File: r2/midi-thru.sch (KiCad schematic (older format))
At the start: 31 parts, among them J1 Barrel_Jack_Switch, J2 MIDI IN, J4 MIDI THRU3, J5 MIDI THRU1, J6 MIDI THRU2, J7 MIDI THRU3, U2 6N138, U3 74HC14

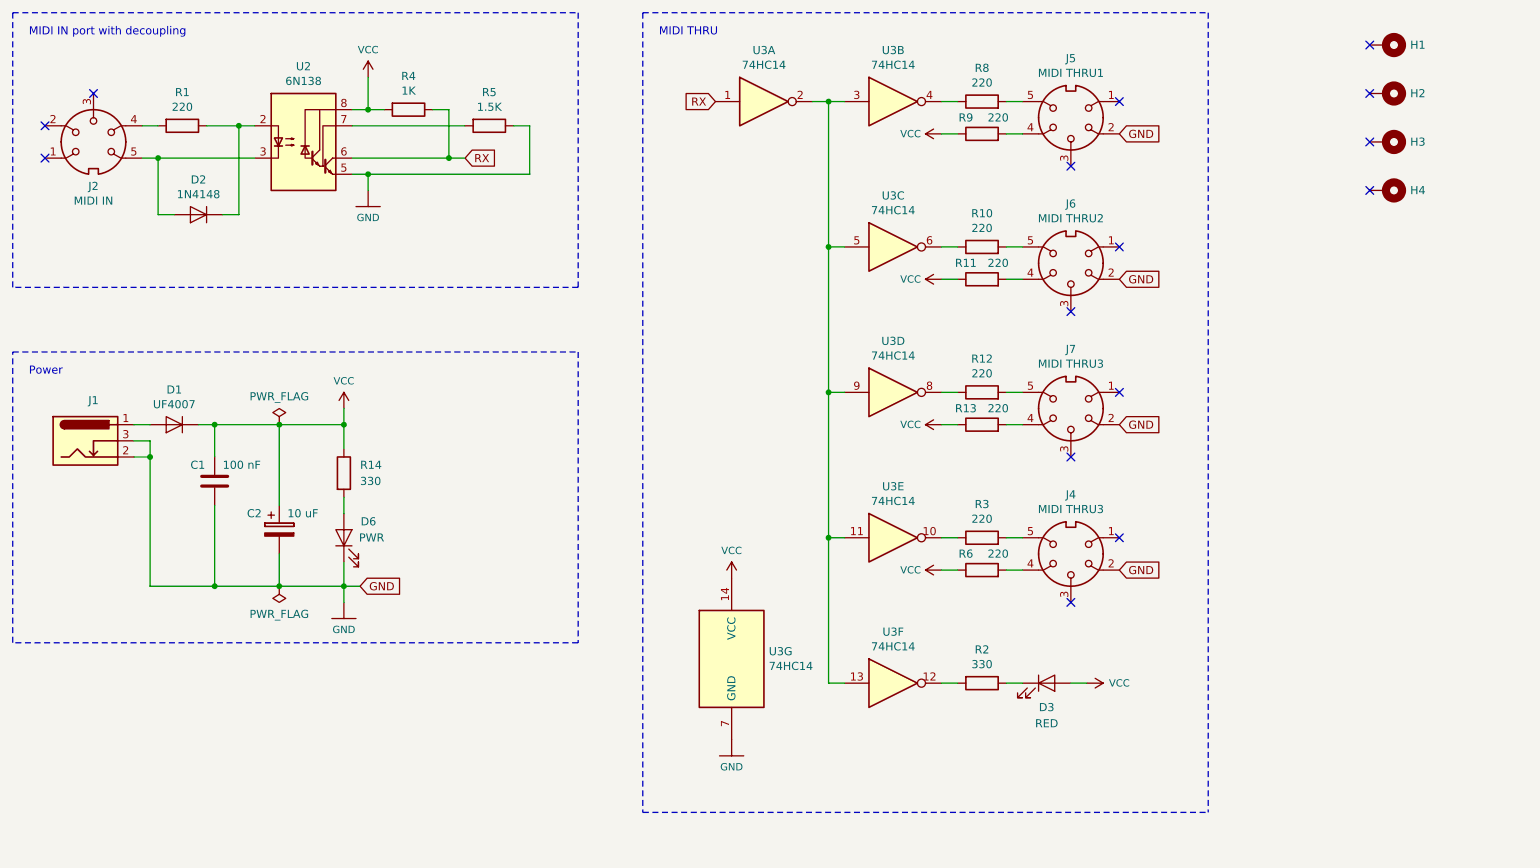
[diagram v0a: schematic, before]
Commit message: Add voltage regulator
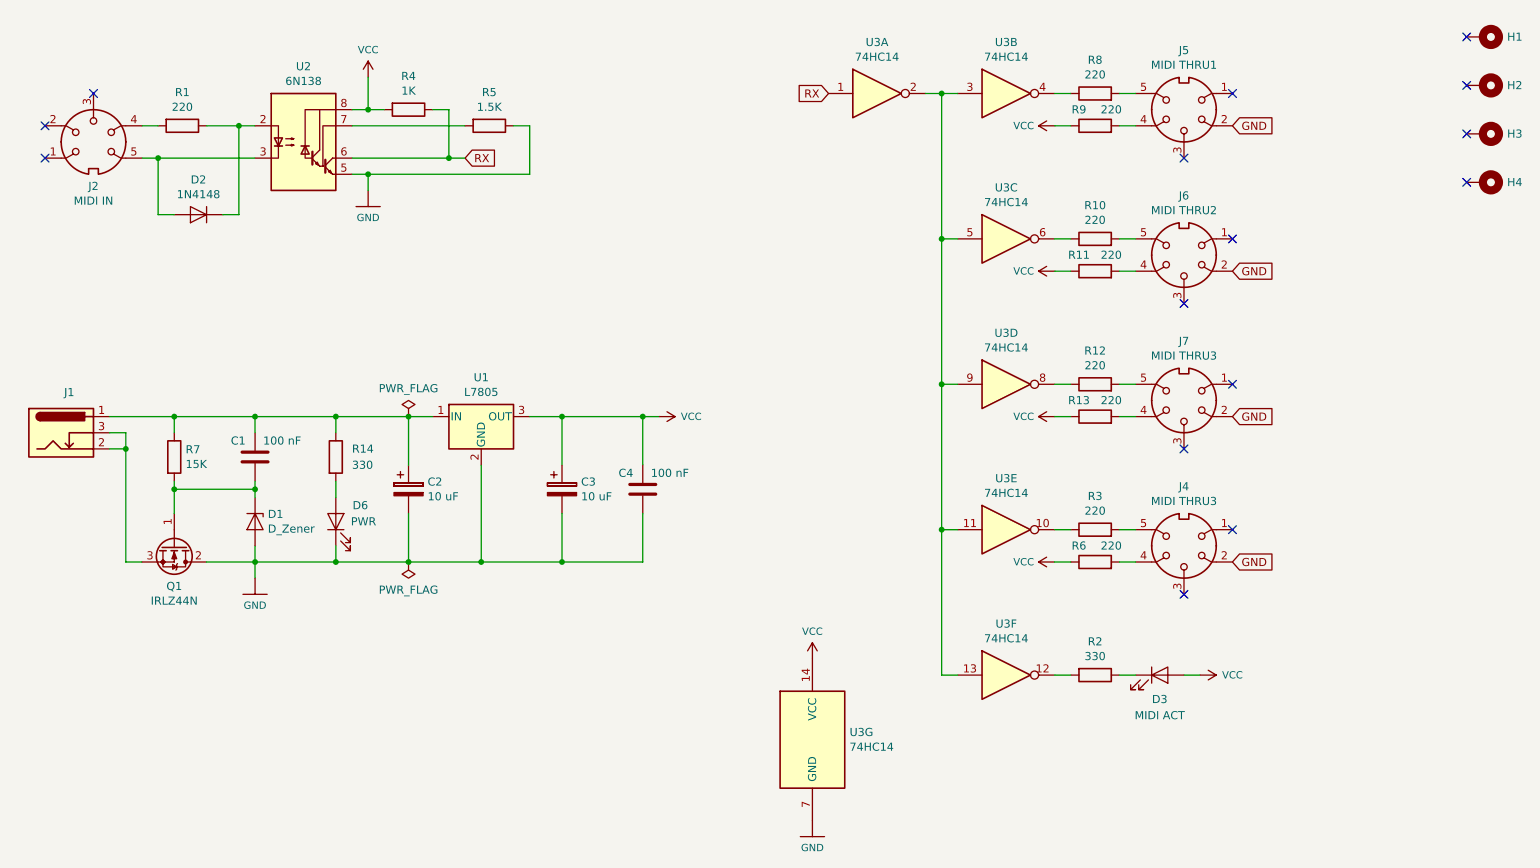
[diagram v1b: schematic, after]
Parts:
- removed D1: UF4007, Diode_THT:D_DO-41_SOD81_P10.16mm_Horizontal, symbol Device:D
- added C3: 10 uF, Capacitor_THT:CP_Radial_D5.0mm_P2.00mm, symbol Device:CP
- added C4: 100 nF, Capacitor_THT:C_Disc_D5.0mm_W2.5mm_P5.00mm, symbol Device:C
- added D1: D_Zener, Diode_THT:D_DO-35_SOD27_P7.62mm_Horizontal, symbol Device:D_Zener
- added Q1: IRLZ44N, Package_TO_SOT_THT:TO-220-3_Vertical, symbol Transistor_FET:IRLZ44N
- added R7: 15K, Resistor_THT:R_Axial_DIN0204_L3.6mm_D1.6mm_P7.62mm_Horizontal, symbol Device:R
- added U1: L7805, Package_TO_SOT_THT:TO-220-3_Vertical, symbol Regulator_Linear:L7805
- C2: footprint Capacitor_THT:CP_Radial_D5.0mm_P2.50mm -> Capacitor_THT:CP_Radial_D5.0mm_P2.00mm
- D3: value RED -> MIDI ACT
- U3: footprint (none) -> Package_DIP:DIP-14_W7.62mm_Socket
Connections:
- net GND: now also C3.2, C4.2, D1.2 (A), Q1.2 (D), U1.2 (GND); no longer C1.2, J1.2, J1.3
- net VCC: now also C3.1, C4.1, U1.3 (OUT); no longer C1.1, C2.1, R14.1
- net at J1.1: now also C1.1, C2.1, R14.1, R7.1, U1.1 (IN)
- new net: J1.2, J1.3, Q1.3 (S)
- new net: C1.2, D1.1 (K), Q1.1 (G), R7.2
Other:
- note removed: "MIDI IN port with decoupling"
- note removed: "MIDI THRU"
- note removed: "Power"
- moved on the sheet: D3, D6, H1, H2, H3, H4, J1, J4, J5, J6, J7, R10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

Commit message: Update PDF schematics
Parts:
- C2, C3: value 10 uF -> 100 uF; footprint Capacitor_THT:CP_Radial_D5.0mm_P2.00mm -> Capacitor_THT:CP_Radial_D6.3mm_P2.50mm
- J6: renamed from J4; value MIDI THRU3 -> MIDI THRU4
- renumbered D2 to D1, D1 to D2, D6 to D3, D3 to D4, J5 to J3, J6 to J4, J7 to J5, R7 to R1, R12 to R10, R13 to R11, R3 to R12, R6 to R13, R2 to R14, R1 to R2, R14 to R3, R8 to R6, R9 to R7, R10 to R8, R11 to R9, U2 to U1, U1 to U2
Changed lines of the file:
@@
 $EndComp
 $Comp
-L Isolator:6N138 U2
+L Isolator:6N138 U1
 U 1 1 5CBC6269
 P 2900 1900
-F 0 "U2" H 2900 2367 50  0000 C CNN
+F 0 "U1" H 2900 2367 50  0000 C CNN
 F 1 "6N138" H 2900 2276 50  0000 C CNN
 F 2 "Package_DIP:DIP-8_W7.62mm_Socket" H 3190 1600 50  0001 C CNN
@@
 $EndComp
 $Comp
-L Device:R R2
+L Device:R R14
 U 1 1 5CBC641E
 P 7800 5200
-F 0 "R2" V 7593 5200 50  0000 C CNN
+F 0 "R14" V 7593 5200 50  0000 C CNN
 F 1 "330" V 7684 5200 50  0000 C CNN
 F 2 "Resistor_THT:R_Axial_DIN0204_L3.6mm_D1.6mm_P7.62mm_Horizontal" V 7730 5200 50  0001 C CNN
@@
 $EndComp
 $Comp
-L Device:LED D3
+L Device:LED D4
 U 1 1 5CBC6A6A
 P 8200 5200
-F 0 "D3" H 8200 5050 50  0000 C CNN
+F 0 "D4" H 8200 5050 50  0000 C CNN
 F 1 "MIDI ACT" H 8200 4950 50  0000 C CNN
 F 2 "LED_THT:LED_D5.0mm" H 8200 5200 50  0001 C CNN
@@
 $EndComp
 $Comp
-L Connector:DIN-5 J6
+L Connector:DIN-5 J4
 U 1 1 5CBC6EF6
 P 8350 2600
-F 0 "J6" H 8350 2233 50  0000 C CNN
+F 0 "J4" H 8350 2233 50  0000 C CNN
 F 1 "MIDI THRU2" H 8350 2324 50  0000 C CNN
 F 2 "turnandpush:din-5" H 8350 2600 50  0001 C CNN
@@
 $EndComp
 $Comp
-L Connector:DIN-5 J5
+L Connector:DIN-5 J3
 U 1 1 5CBC701D
 P 8350 1700
-F 0 "J5" H 8350 1333 50  0000 C CNN
+F 0 "J3" H 8350 1333 50  0000 C CNN
 F 1 "MIDI THRU1" H 8350 1424 50  0000 C CNN
 F 2 "turnandpush:din-5" H 8350 1700 50  0001 C CNN
@@
 GND
 $Comp
-L SparkFun-PowerSymbols:GND #GND05
+L SparkFun-PowerSymbols:GND #GND03
 U 1 1 5CBD0314
 P 6050 6100
-F 0 "#GND05" H 6100 6050 45  0001 L BNN
+F 0 "#GND03" H 6100 6050 45  0001 L BNN
 F 1 "GND" H 6050 5931 45  0000 C CNN
 F 2 "" H 6050 6000 60  0001 C CNN
@@
 $EndComp
 $Comp
-L SparkFun-PowerSymbols:VCC #SUPPLY04
+L SparkFun-PowerSymbols:VCC #SUPPLY03
 U 1 1 5CBD05C9
 P 6050 5100
-F 0 "#SUPPLY04" H 6100 5100 45  0001 L BNN
+F 0 "#SUPPLY03" H 6100 5100 45  0001 L BNN
 F 1 "VCC" H 6050 5270 45  0000 C CNN
 F 2 "XXX-00000" H 6050 5281 60  0001 C CNN
@@
 $EndComp
 $Comp
-L Device:R R1
+L Device:R R2
 U 1 1 5CBD1646
 P 2150 1800
-F 0 "R1" V 1943 1800 50  0000 C CNN
+F 0 "R2" V 1943 1800 50  0000 C CNN
 F 1 "220" V 2034 1800 50  0000 C CNN
 F 2 "Resistor_THT:R_Axial_DIN0204_L3.6mm_D1.6mm_P7.62mm_Horizontal" V 2080 1800 50  0001 C CNN
@@
 $EndComp
 $Comp
-L Device:D D2
+L Device:D D1
 U 1 1 5CBD1A75
 P 2250 2350
-F 0 "D2" H 2250 2134 50  0000 C CNN
+F 0 "D1" H 2250 2134 50  0000 C CNN
 F 1 "1N4148" H 2250 2225 50  0000 C CNN
 F 2 "Diode_THT:D_DO-35_SOD27_P7.62mm_Horizontal" H 2250 2350 50  0001 C CNN
@@
 	2500 1800 2600 1800
 $Comp
-L SparkFun-PowerSymbols:VCC #SUPPLY02
+L SparkFun-PowerSymbols:VCC #SUPPLY01
 U 1 1 5CBD721F
 P 3300 1500
-F 0 "#SUPPLY02" H 3350 1500 45  0001 L BNN
+F 0 "#SUPPLY01" H 3350 1500 45  0001 L BNN
 F 1 "VCC" H 3300 1670 45  0000 C CNN
 F 2 "XXX-00000" H 3300 1681 60  0001 C CNN
@@
 Connection ~ 3800 2000
 $Comp
-L Device:R R8
+L Device:R R6
 U 1 1 5CBEDF49
 P 7800 1600
-F 0 "R8" V 8007 1600 50  0000 C CNN
+F 0 "R6" V 8007 1600 50  0000 C CNN
 F 1 "220" V 7916 1600 50  0000 C CNN
 F 2 "Resistor_THT:R_Axial_DIN0204_L3.6mm_D1.6mm_P7.62mm_Horizontal" V 7730 1600 50  0001 C CNN
@@
 $EndComp
 $Comp
-L Device:R R10
+L Device:R R8
 U 1 1 5CC0A6C8
 P 7800 2500
-F 0 "R10" V 8007 2500 50  0000 C CNN
+F 0 "R8" V 8007 2500 50  0000 C CNN
 F 1 "220" V 7916 2500 50  0000 C CNN
 F 2 "Resistor_THT:R_Axial_DIN0204_L3.6mm_D1.6mm_P7.62mm_Horizontal" V 7730 2500 50  0001 C CNN
@@
 $EndComp
 $Comp
-L Device:R R9
+L Device:R R7
 U 1 1 5CC34AB7
 P 7800 1800
-F 0 "R9" V 7900 1900 50  0000 C CNN
+F 0 "R7" V 7900 1900 50  0000 C CNN
 F 1 "220" V 7900 1700 50  0000 C CNN
 F 2 "Resistor_THT:R_Axial_DIN0204_L3.6mm_D1.6mm_P7.62mm_Horizontal" V 7730 1800 50  0001 C CNN
@@
 $EndComp
 $Comp
-L SparkFun-PowerSymbols:VCC #SUPPLY06
+L SparkFun-PowerSymbols:VCC #SUPPLY04
 U 1 1 5CC34ABE
 P 7550 1800
-F 0 "#SUPPLY06" H 7600 1800 45  0001 L BNN
+F 0 "#SUPPLY04" H 7600 1800 45  0001 L BNN
 F 1 "VCC" V 7550 1928 45  0000 L CNN
 F 2 "XXX-00000" H 7550 1981 60  0001 C CNN
@@
 $EndComp
 $Comp
-L Device:R R11
+L Device:R R9
 U 1 1 5CC35E70
 P 7800 2700
-F 0 "R11" V 7900 2800 50  0000 C CNN
+F 0 "R9" V 7900 2800 50  0000 C CNN
 F 1 "220" V 7900 2600 50  0000 C CNN
 F 2 "Resistor_THT:R_Axial_DIN0204_L3.6mm_D1.6mm_P7.62mm_Horizontal" V 7730 2700 50  0001 C CNN
@@
 $EndComp
 $Comp
-L SparkFun-PowerSymbols:VCC #SUPPLY07
+L SparkFun-PowerSymbols:VCC #SUPPLY05
 U 1 1 5CC35E77
 P 7550 2700
-F 0 "#SUPPLY07" H 7600 2700 45  0001 L BNN
+F 0 "#SUPPLY05" H 7600 2700 45  0001 L BNN
 F 1 "VCC" V 7550 2828 45  0000 L CNN
 F 2 "XXX-00000" H 7550 2881 60  0001 C CNN
@@
 	6850 1600 6950 1600
 $Comp
-L Connector:DIN-5 J7
+L Connector:DIN-5 J5
 U 1 1 5CC58EAE
 P 8350 3500
-F 0 "J7" H 8350 3133 50  0000 C CNN
+F 0 "J5" H 8350 3133 50  0000 C CNN
 F 1 "MIDI THRU3" H 8350 3224 50  0000 C CNN
 F 2 "turnandpush:din-5" H 8350 3500 50  0001 C CNN
@@
 GND
 $Comp
-L Device:R R12
+L Device:R R10
 U 1 1 5CC58EB8
 P 7800 3400
-F 0 "R12" V 8007 3400 50  0000 C CNN
+F 0 "R10" V 8007 3400 50  0000 C CNN
 F 1 "220" V 7916 3400 50  0000 C CNN
 F 2 "Resistor_THT:R_Axial_DIN0204_L3.6mm_D1.6mm_P7.62mm_Horizontal" V 7730 3400 50  0001 C CNN
@@
 $EndComp
 $Comp
-L Device:R R13
+L Device:R R11
 U 1 1 5CC58EBF
 P 7800 3600
-F 0 "R13" V 7900 3700 50  0000 C CNN
+F 0 "R11" V 7900 3700 50  0000 C CNN
 F 1 "220" V 7900 3500 50  0000 C CNN
 F 2 "Resistor_THT:R_Axial_DIN0204_L3.6mm_D1.6mm_P7.62mm_Horizontal" V 7730 3600 50  0001 C CNN
@@
 $EndComp
 $Comp
-L SparkFun-PowerSymbols:VCC #SUPPLY08
+L SparkFun-PowerSymbols:VCC #SUPPLY06
 U 1 1 5CC58EC6
 P 7550 3600
-F 0 "#SUPPLY08" H 7600 3600 45  0001 L BNN
+F 0 "#SUPPLY06" H 7600 3600 45  0001 L BNN
 F 1 "VCC" V 7550 3728 45  0000 L CNN
 F 2 "XXX-00000" H 7550 3781 60  0001 C CNN
@@
 $EndComp
 $Comp
-L Device:R R14
+L Device:R R3
 U 1 1 5CBEEE77
 P 3100 3850
-F 0 "R14" H 3200 3900 50  0000 L CNN
+F 0 "R3" H 3200 3900 50  0000 L CNN
 F 1 "330" H 3200 3800 50  0000 L CNN
 F 2 "Resistor_THT:R_Axial_DIN0204_L3.6mm_D1.6mm_P7.62mm_Horizontal" V 3030 3850 50  0001 C CNN
@@
 $EndComp
 $Comp
-L Device:LED D6
+L Device:LED D3
 U 1 1 5CBEEE7E
 P 3100 4250
-F 0 "D6" V 3200 4050 50  0000 L CNN
+F 0 "D3" V 3200 4050 50  0000 L CNN
 F 1 "PWR" V 3100 4000 50  0000 L CNN
 F 2 "LED_THT:LED_D5.0mm" H 3100 4250 50  0001 C CNN
@@
 $EndComp
 $Comp
-L Connector:DIN-5 J4
+L Connector:DIN-5 J6
 U 1 1 5CC7D072
 P 8350 4400
-F 0 "J4" H 8350 4033 50  0000 C CNN
-F 1 "MIDI THRU3" H 8350 4124 50  0000 C CNN
+F 0 "J6" H 8350 4033 50  0000 C CNN
+F 1 "MIDI THRU4" H 8350 4124 50  0000 C CNN
 F 2 "turnandpush:din-5" H 8350 4400 50  0001 C CNN
 F 3 "http://www.mouser.com/ds/2/18/40_c091_abd_e-75918.pdf" H 8350 4400 50  0001 C CNN
@@
 GND
 $Comp
-L Device:R R3
+L Device:R R12
 U 1 1 5CC7D07C
 P 7800 4300
-F 0 "R3" V 8007 4300 50  0000 C CNN
+F 0 "R12" V 8007 4300 50  0000 C CNN
 F 1 "220" V 7916 4300 50  0000 C CNN
 F 2 "Resistor_THT:R_Axial_DIN0204_L3.6mm_D1.6mm_P7.62mm_Horizontal" V 7730 4300 50  0001 C CNN
@@
 $EndComp
 $Comp
-L Device:R R6
+L Device:R R13
 U 1 1 5CC7D083
 P 7800 4500
-F 0 "R6" V 7900 4600 50  0000 C CNN
+F 0 "R13" V 7900 4600 50  0000 C CNN
 F 1 "220" V 7900 4400 50  0000 C CNN
 F 2 "Resistor_THT:R_Axial_DIN0204_L3.6mm_D1.6mm_P7.62mm_Horizontal" V 7730 4500 50  0001 C CNN
@@
 $EndComp
 $Comp
-L SparkFun-PowerSymbols:VCC #SUPPLY03
+L SparkFun-PowerSymbols:VCC #SUPPLY07
 U 1 1 5CC7D08A
 P 7550 4500
-F 0 "#SUPPLY03" H 7600 4500 45  0001 L BNN
+F 0 "#SUPPLY07" H 7600 4500 45  0001 L BNN
 F 1 "VCC" V 7550 4628 45  0000 L CNN
 F 2 "XXX-00000" H 7550 4681 60  0001 C CNN
@@
 Connection ~ 6850 4300
 $Comp
-L SparkFun-PowerSymbols:VCC #SUPPLY05
+L SparkFun-PowerSymbols:VCC #SUPPLY08
 U 1 1 5CC86D5F
 P 8450 5200
-F 0 "#SUPPLY05" H 8500 5200 45  0001 L BNN
+F 0 "#SUPPLY08" H 8500 5200 45  0001 L BNN
 F 1 "VCC" V 8450 5400 45  0000 C CNN
 F 2 "XXX-00000" H 8450 5381 60  0001 C CNN
@@
 Connection ~ 6850 3400
 $Comp
-L Regulator_Linear:L7805 U1
+L Regulator_Linear:L7805 U2
 U 1 1 5CC76B3C
 P 4000 3600
-F 0 "U1" H 4000 3842 50  0000 C CNN
+F 0 "U2" H 4000 3842 50  0000 C CNN
 F 1 "L7805" H 4000 3751 50  0000 C CNN
 F 2 "Package_TO_SOT_THT:TO-220-3_Vertical" H 4025 3450 50  0001 L CIN
@@
 P 3550 4050
 F 0 "C2" H 3668 4096 50  0000 L CNN
-F 1 "10 uF" H 3668 4005 50  0000 L CNN
-F 2 "Capacitor_THT:CP_Radial_D5.0mm_P2.00mm" H 3588 3900 50  0001 C CNN
+F 1 "100 uF" H 3668 4005 50  0000 L CNN
+F 2 "Capacitor_THT:CP_Radial_D6.3mm_P2.50mm" H 3588 3900 50  0001 C CNN
 F 3 "~" H 3550 4050 50  0001 C CNN
 	1    3550 4050
@@
 P 4500 4050
 F 0 "C3" H 4618 4096 50  0000 L CNN
-F 1 "10 uF" H 4618 4005 50  0000 L CNN
-F 2 "Capacitor_THT:CP_Radial_D5.0mm_P2.00mm" H 4538 3900 50  0001 C CNN
+F 1 "100 uF" H 4618 4005 50  0000 L CNN
+F 2 "Capacitor_THT:CP_Radial_D6.3mm_P2.50mm" H 4538 3900 50  0001 C CNN
 F 3 "~" H 4500 4050 50  0001 C CNN
 	1    4500 4050
@@
 $EndComp
 $Comp
-L Device:R R7
+L Device:R R1
 U 1 1 5CC79BBB
 P 2100 3850
-F 0 "R7" H 2170 3896 50  0000 L CNN
+F 0 "R1" H 2170 3896 50  0000 L CNN
 F 1 "15K" H 2170 3805 50  0000 L CNN
 F 2 "Resistor_THT:R_Axial_DIN0204_L3.6mm_D1.6mm_P7.62mm_Horizontal" V 2030 3850 50  0001 C CNN
@@
 $EndComp
 $Comp
-L Device:D_Zener D1
+L Device:D_Zener D2
 U 1 1 5CC7ADF7
 P 2600 4250
-F 0 "D1" V 2554 4329 50  0000 L CNN
+F 0 "D2" V 2554 4329 50  0000 L CNN
 F 1 "D_Zener" V 2645 4329 50  0000 L CNN
 F 2 "Diode_THT:D_DO-35_SOD27_P7.62mm_Horizontal" H 2600 4250 50  0001 C CNN
@@
 Connection ~ 4500 4500
 $Comp
-L SparkFun-PowerSymbols:VCC #SUPPLY01
+L SparkFun-PowerSymbols:VCC #SUPPLY02
 U 1 1 5CCA9C8C
 P 5100 3600
-F 0 "#SUPPLY01" H 5150 3600 45  0001 L BNN
+F 0 "#SUPPLY02" H 5150 3600 45  0001 L BNN
 F 1 "VCC" V 5100 3800 45  0000 C CNN
 F 2 "XXX-00000" H 5100 3781 60  0001 C CNN
